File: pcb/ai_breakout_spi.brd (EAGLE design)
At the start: 12.7 x 10.2 mm, 3 parts, among them J1 2X03, J2 1X03, J3 1X03NOFIRST

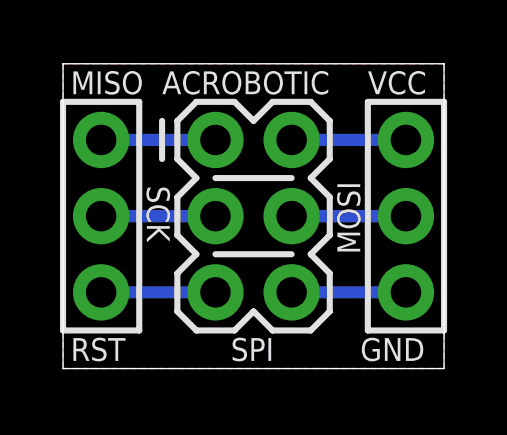
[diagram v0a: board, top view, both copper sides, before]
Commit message: revising silly mistakes on silkscreen
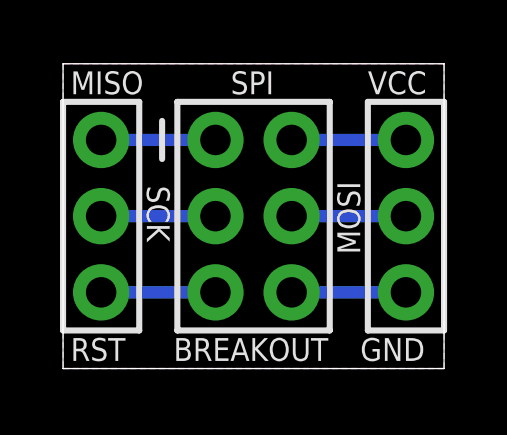
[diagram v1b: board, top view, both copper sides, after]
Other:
- board text added: "BREAKOUT"
- board text added: "Pasadena, CA"
- board text added: "v1.1"
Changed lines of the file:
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@@
 <?xml version="1.0" encoding="utf-8"?>
 <!DOCTYPE eagle SYSTEM "eagle.dtd">
-<eagle version="7.1.0">
+<eagle version="6.5.0">
 <drawing>
 <settings>
@@
 <setting verticaltext="up"/>
 </settings>
-<grid distance="50" unitdist="mil" unit="mil" style="lines" multiple="1" display="yes" altdistance="0.025" altunitdist="inch" altunit="inch"/>
+<grid distance="10" unitdist="mil" unit="mil" style="lines" multiple="1" display="yes" altdistance="0.025" altunitdist="inch" altunit="inch"/>
 <layers>
 <layer number="1" name="Top" color="4" fill="1" visible="yes" active="yes"/>
@@
 <wire x1="12.7" y1="0" x2="12.7" y2="10.16" width="0.0254" layer="20"/>
 <wire x1="12.7" y1="10.16" x2="0" y2="10.16" width="0.0254" layer="20"/>
-<text x="0.254" y="9.144" size="0.762" layer="25" font="vector" ratio="15">MISO</text>
-<text x="10.16" y="9.144" size="0.762" layer="25" font="vector" ratio="15">VCC</text>
-<text x="0.254" y="0.254" size="0.762" layer="25" font="vector" ratio="15">RST</text>
-<text x="9.906" y="0.254" size="0.762" layer="25" font="vector" ratio="15">GND</text>
-<text x="2.794" y="6.096" size="0.762" layer="25" font="vector" ratio="15" rot="SR270">SCK</text>
-<text x="9.906" y="3.81" size="0.762" layer="25" font="vector" ratio="15" rot="SR90">MOSI</text>
-<text x="3.302" y="9.144" size="0.762" layer="25" font="vector" ratio="15">ACROBOTIC</text>
-<text x="5.588" y="0.254" size="0.762" layer="25" font="vector" ratio="15">SPI</text>
+<text x="0.254" y="9.144" size="0.762" layer="25" font="vector" ratio="10">MISO</text>
+<text x="10.16" y="9.144" size="0.762" layer="25" font="vector" ratio="10">VCC</text>
+<text x="0.254" y="0.254" size="0.762" layer="25" font="vector" ratio="10">RST</text>
+<text x="9.906" y="0.254" size="0.762" layer="25" font="vector" ratio="10">GND</text>
+<text x="2.794" y="6.096" size="0.762" layer="25" font="vector" ratio="10" rot="SR270">SCK</text>
+<text x="9.906" y="3.81" size="0.762" layer="25" font="vector" ratio="10" rot="SR90">MOSI</text>
+<text x="3.048" y="9.906" size="0.762" layer="26" font="vector" ratio="10" rot="MR180">ACROBOTIC</text>
+<text x="5.588" y="9.144" size="0.762" layer="25" font="vector" ratio="10">SPI</text>
+<text x="2.159" y="1.016" size="0.762" layer="26" font="vector" ratio="10" rot="MR180">Pasadena, CA</text>
+<text x="3.683" y="0.254" size="0.762" layer="25" font="vector" ratio="10">BREAKOUT</text>
+<text x="0" y="9.906" size="0.762" layer="26" font="vector" ratio="10" rot="MR180">v1.1</text>
 </plain>
 <attributes>
@@
 <pass name="Default">
 <param name="RoutingGrid" value="50mil"/>
-<param name="AutoGrid" value="1"/>
-<param name="Efforts" value="0"/>
-<param name="TopRouterVariant" value="1"/>
 <param name="tpViaShape" value="round"/>
-<param name="PrefDir.1" value="a"/>
+<param name="PrefDir.1" value="|"/>
 <param name="PrefDir.2" value="0"/>
 <param name="PrefDir.3" value="0"/>
@@
 <param name="PrefDir.14" value="0"/>
 <param name="PrefDir.15" value="0"/>
-<param name="PrefDir.16" value="a"/>
+<param name="PrefDir.16" value="-"/>
 <param name="cfVia" value="8"/>
 <param name="cfNonPref" value="5"/>
